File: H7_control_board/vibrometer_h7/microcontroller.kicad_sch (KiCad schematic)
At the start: 34 parts, among them J201 Conn_01x04_Socket, J202 Conn_02x06, J204 TC2030-NL, Q201 BSS138, Q202 BSS138, Q203 BSS138, SW201 SW_Push, U201 STM32H723VGTx, Y201 24MHz

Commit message: connectors, they are so BIG whyyyy john, whyyy
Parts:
- R201, R202, R203, R204, R206, R207, R208: footprint Resistor_SMD:R_0603_1608Metric -> Resistor_SMD:R_0402_1005Metric

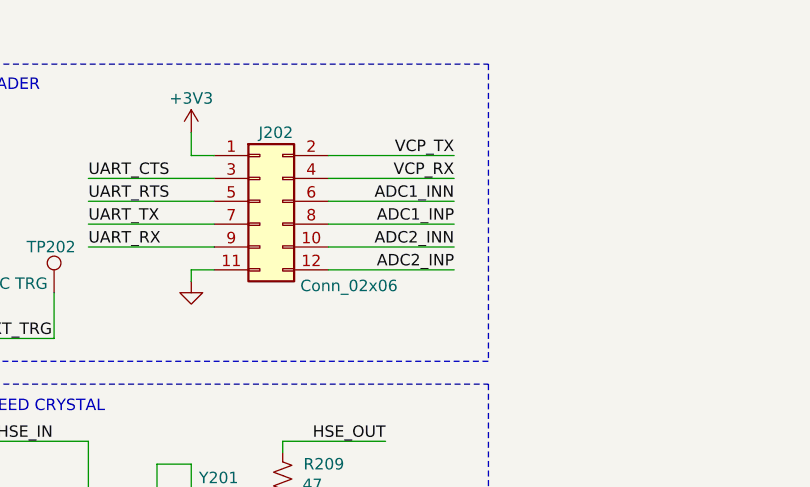
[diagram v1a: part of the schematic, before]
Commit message: some rerouting, cleaned up silkscreen
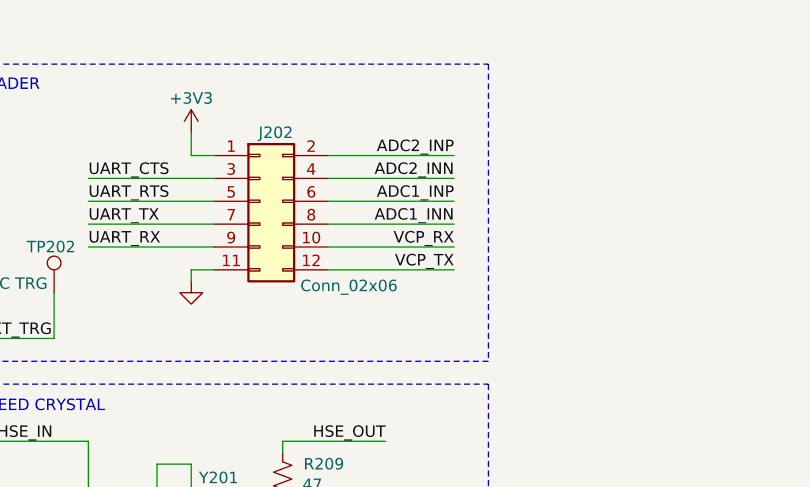
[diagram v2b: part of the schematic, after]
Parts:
- J202: footprint Connector_PinHeader_1.00mm:PinHeader_2x06_P1.00mm_Vertical_SMD -> Connector_PinHeader_2.54mm:PinHeader_2x06_P2.54mm_Vertical
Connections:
- net ADC1_INN: now also J202.8 (Pin_8); no longer J202.6 (Pin_6)
- net ADC1_INP: now also J202.6 (Pin_6); no longer J202.8 (Pin_8)
- net ADC2_INN: now also J202.4 (Pin_4); no longer J202.10 (Pin_10)
- net ADC2_INP: now also J202.2 (Pin_2); no longer J202.12 (Pin_12)
- net VCP_RX: now also J202.10 (Pin_10); no longer J202.4 (Pin_4)
- net VCP_TX: now also J202.12 (Pin_12); no longer J202.2 (Pin_2)

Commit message: nearly done....
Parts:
- added TP203: GPIO_timing1, TestPoint:TestPoint_Pad_D1.0mm, symbol Connector:TestPoint
- added TP204: GPIO_timing2, TestPoint:TestPoint_Pad_D1.0mm, symbol Connector:TestPoint
- C202, C203, C205, C207, C208, C209, C210, C211: footprint Capacitor_SMD:C_0402_1005Metric_Pad0.74x0.62mm_HandSolder -> Capacitor_SMD:C_0402_1005Metric
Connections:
- net at U201.17 (PC2_C): now also TP204.1
- net at U201.22 (PA0): now also TP203.1
- no-connect marks 33 -> 31
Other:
- note added: "- CHECK CRYSTAL FOOTPRINT"
- note added: "- PICK COLORS FOR MUTE / RECORD LEDS, CHANGE LCSC PARTS TO MATCH"
- note added: "AMPLIFIER SAYS SOIC-8, USING SSOP-8 FOOTPRINT? CHECK THIS!"
- note added: "CHECK PUSH SWITCH FOOTPRINT SIZE / CONNECTION"
- note added: "EDIT FOOTPRINT FOR LED SWITCHING FETS"
- note added: "SPEC RESISTOR VAL FOR STROBE LED CURRENT LIM"
- note removed: "ADD MUTE AND RECORD INDICATOR LED PINS TO CUBE IDE"
- note removed: "CHANGE TO 2X6 1.27MM PITCH SMD HEADER"
- note removed: "CHECK DATASHESET FOR IF BOOT SHOULD BE DEBOUNCED"
- note removed: "LOOK FOR ALL IN ONE LEVEL SHIFTER IC FOR THESE"
- note removed: "PICK COLORS FOR MUTE / RECORD LEDS, CHANGE LCSC PARTS TO MATCH"
- note removed: "SEE IF DEBOUNCING IS NECESSARY? DO IT WITH INTERNAL PULL-UP AND SOFTWARE DEBOUNCE"
- note removed: "SPEC COMPONENTS FOR LED SWITCHING FETS AND LED RESISTORS"

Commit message: checked all footprints, made tiny daughterboard
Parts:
- J202: now not fitted
- R209: footprint Resistor_SMD:R_0603_1608Metric -> Resistor_SMD:R_0402_1005Metric; LCSC C23182 -> (none)
- SW201: LCSC C3010224 -> C221872
- Y201: footprint Crystal:Crystal_SMD_2016-4Pin_2.0x1.6mm -> Crystal:Crystal_SMD_3225-4Pin_3.2x2.5mm; LCSC C2965584 -> C70590
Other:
- note added: "- AMPLIFIER SAYS SOIC-8, USING SSOP-8 FOOTPRINT? CHECK THIS!"
- note added: "- CHECK PUSH SWITCH FOOTPRINT SIZE / CONNECTION"
- note added: "- EDIT FOOTPRINT FOR LED SWITCHING FETS"
- note removed: "AMPLIFIER SAYS SOIC-8, USING SSOP-8 FOOTPRINT? CHECK THIS!"
- note removed: "CHECK PUSH SWITCH FOOTPRINT SIZE / CONNECTION"
- note removed: "EDIT FOOTPRINT FOR LED SWITCHING FETS"

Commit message: boards sent to JLCPCB!
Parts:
- R209: LCSC (none) -> C25118
